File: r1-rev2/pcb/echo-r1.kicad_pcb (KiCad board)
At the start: 6 copper layers, 90.8 x 100.6 mm, 146 parts, among them J1 TYPE-C-31-M-12, J2 TF-115, J3 HP_3.5mm, J4 LO_3.5mm, J5 GT-BTP30003-xxxA-16A, J6 AFC07-S30ECA-00, Q1 AO3401A, Q2 AO3401A, Q3 AO3401A, Q4 AO3401A, Q5 AO3401A, SW1 A, SW10 SELECT, SW11 VOL+, SW12 VOL-, SW13 POWER, SW14 HOLD, SW2 B, SW3 X, SW4 Y, SW5 DPAD↑, SW6 DPAD↓, SW7 DPAD←, SW8 DPAD→, SW9 START, U1 STM32H7R3Z8Jx, U10 USBLC6-2SC6, U11 TPAZ1143-04F, U12 TPAZ1143-04F, U15 TPAZ1143-04F, U16 TPAZ1143-04F, U2 W958D8NBYA5I, U3 TLV320AIC3104, U4 LM66100DCK, U5 TPS62A01DRLR, U6 TPS62A01DRLR, U7 AP2125K-3.0, U8 AP2125K-3.0, U9 TP4057, Y1 SC-32S32.768kHz20PPM12.5pF, Y2 XTM32024000JT00351001

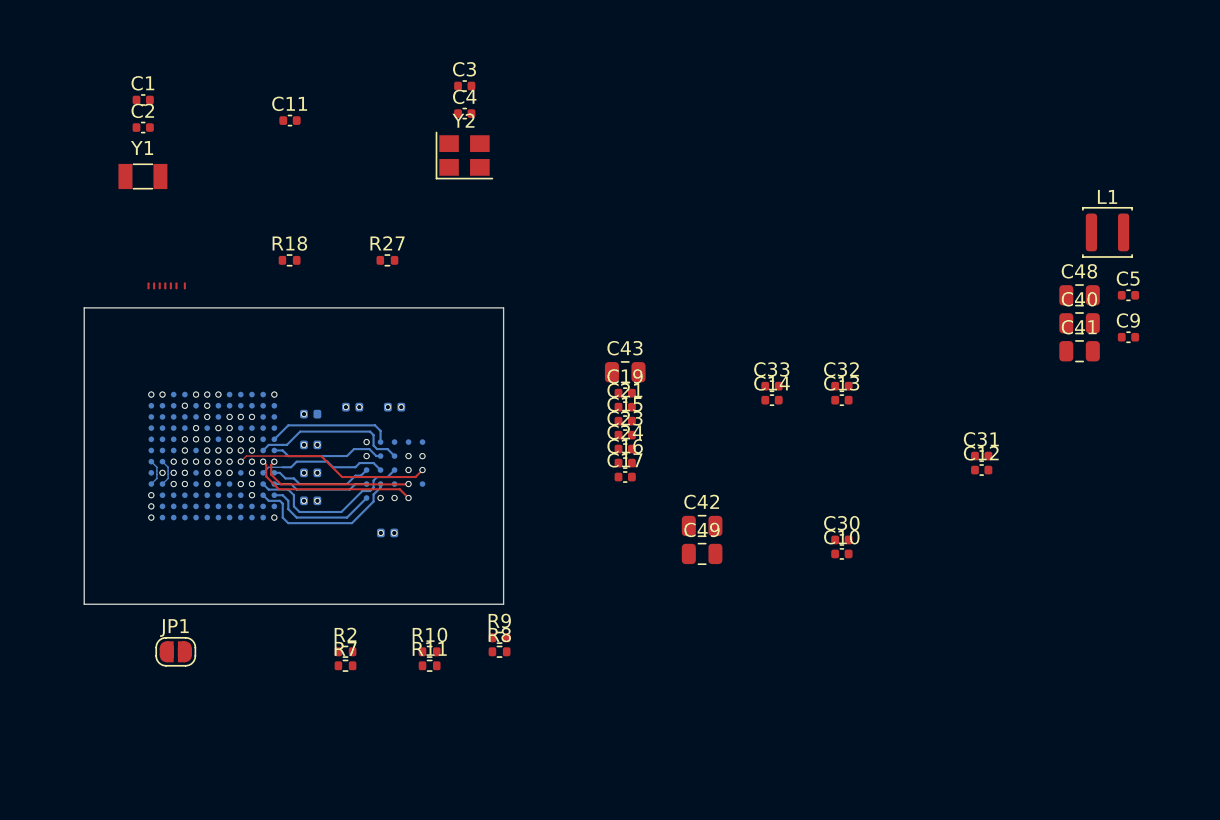
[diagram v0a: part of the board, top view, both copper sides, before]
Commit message: R1-Rev2: WIP STM32 crystal and SMPS layout
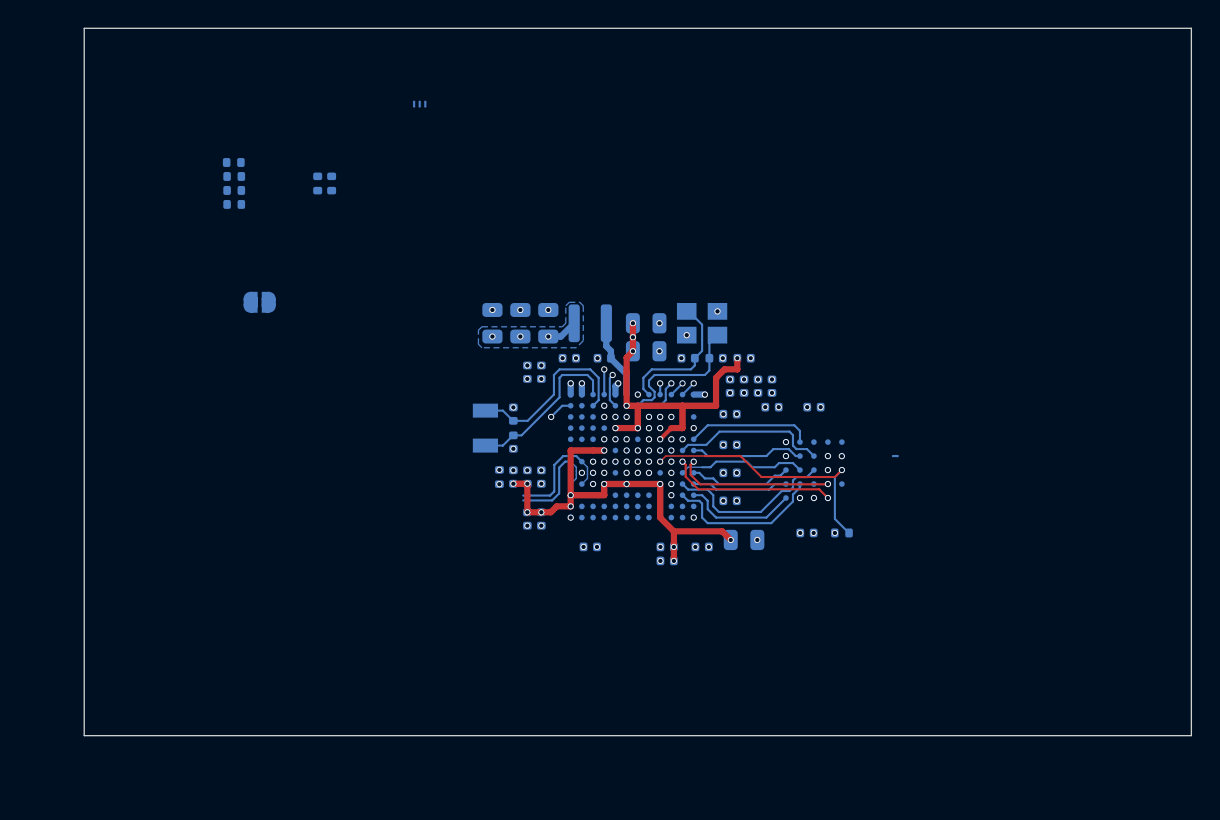
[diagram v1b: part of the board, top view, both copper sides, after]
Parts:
- removed NT10, NT4, NT5: NetTie_2, echoplayer:NetTie_0.15mm_SMD
- C1, C10, C11, C12, C13, C14, C15, C16, C17, C19, C2, C21, C23, C24, C3, C30, C31, C32, C33, C4, C40, C41, C42, C43, C48, C49, C5, C9, JP1, L1, NT1, NT11, NT6, NT7, R10, R11, R18, R2, R27, R7, R8, R9, Y1, Y2: moved to B.Cu
- moved NT11 52.3 mm to (240.3, 62.0), turned to 180 degrees
- moved C9 43.2 mm to (215.0, 63.5), turned to -90 degrees
- moved C11 42.4 mm to (226.5, 68.5)
- moved C41 42.0 mm to (211.5, 52.5), turned to 90 degrees
- moved C40 40.0 mm to (213.5, 52.5), turned to 90 degrees
- moved C48 38.1 mm to (215.5, 52.5), turned to 90 degrees
- moved R27 37.9 mm to (236.5, 67.5)
- moved C5 37.8 mm to (219.5, 55.0), turned to 180 degrees
- moved L1 37.6 mm to (218.5, 52.5)
- moved C1 36.1 mm to (213.0, 61.0), turned to -90 degrees
- moved R2 35.9 mm to (193.0, 41.0)
- moved R7 35.9 mm to (193.0, 42.0), turned to 180 degrees
- moved R10 35.8 mm to (193.0, 43.0), turned to 180 degrees
- moved R11 35.8 mm to (193.0, 44.0), turned to 180 degrees
- moved R8 35.6 mm to (200.0, 42.5), turned to -90 degrees
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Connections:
- U1 pad C8: /dvdd -> /vfbsmps
- U1 pad E5: /vcap -> /vfbsmps
- U1 pad F6: /vddldo -> /vfbsmps
- U1 pad F7: /vddldo -> /vfbsmps
- U1 pad F8: /vcap -> /vfbsmps
- U1 pad G6: /vddldo -> /vfbsmps
- U1 pad G7: /vddldo -> /vfbsmps
- U1 pad H6: /vcap -> /vfbsmps
- U1 pad H8: /vcap -> /vfbsmps
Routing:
- net +3V3: track 0.00 -> 53.9 mm, vias 10 -> 23
- net /vfbsmps: track 0.00 -> 32.9 mm, vias 1 -> 14
- net +1V8: track 26.2 -> 39.5 mm, vias 13 -> 14
- net /osc32k_out: track 0.00 -> 13.2 mm
- net +3V0_VBAT: track 0.00 -> 11.8 mm, vias 3 -> 9
- net /osc32k_in: track 0.00 -> 11.8 mm
- net /osc24m_in: track 0.00 -> 10.2 mm
- net /osc24m_out: track 0.00 -> 10.0 mm
- net /usb_d-: track 0.84 -> 7.48 mm
- net /vlxsmps: track 0.00 -> 5.70 mm, vias 1 -> 0
- net /usb_d+: track 0.84 -> 6.47 mm
- net /xspi.cs: track 14.0 -> 19.1 mm
- net GND: track 0.00 -> 2.48 mm, vias 30 -> 62
- net /codec.dplay: track 0.00 -> 2.45 mm, vias 0 -> 1
- net /lcd.d6: track 0.00 -> 1.93 mm, vias 0 -> 1
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- added copper zone on B.Cu, net /vfbsmps
- added copper zone on In3.Cu, net /vfbsmps
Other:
- board size 90.8 x 100.6 mm -> 140 x 120.6 mm

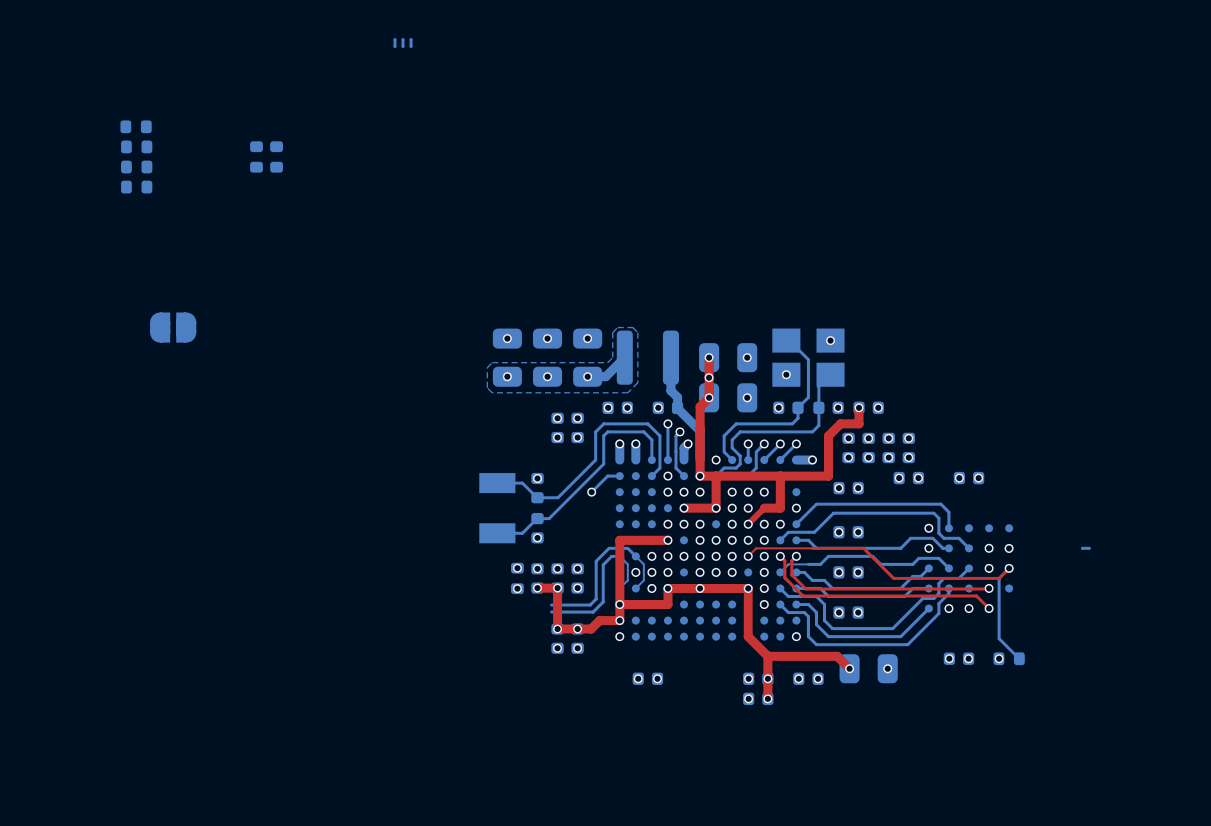
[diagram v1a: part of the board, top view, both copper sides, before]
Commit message: R1-Rev2: WIP STM32 signal and power routing
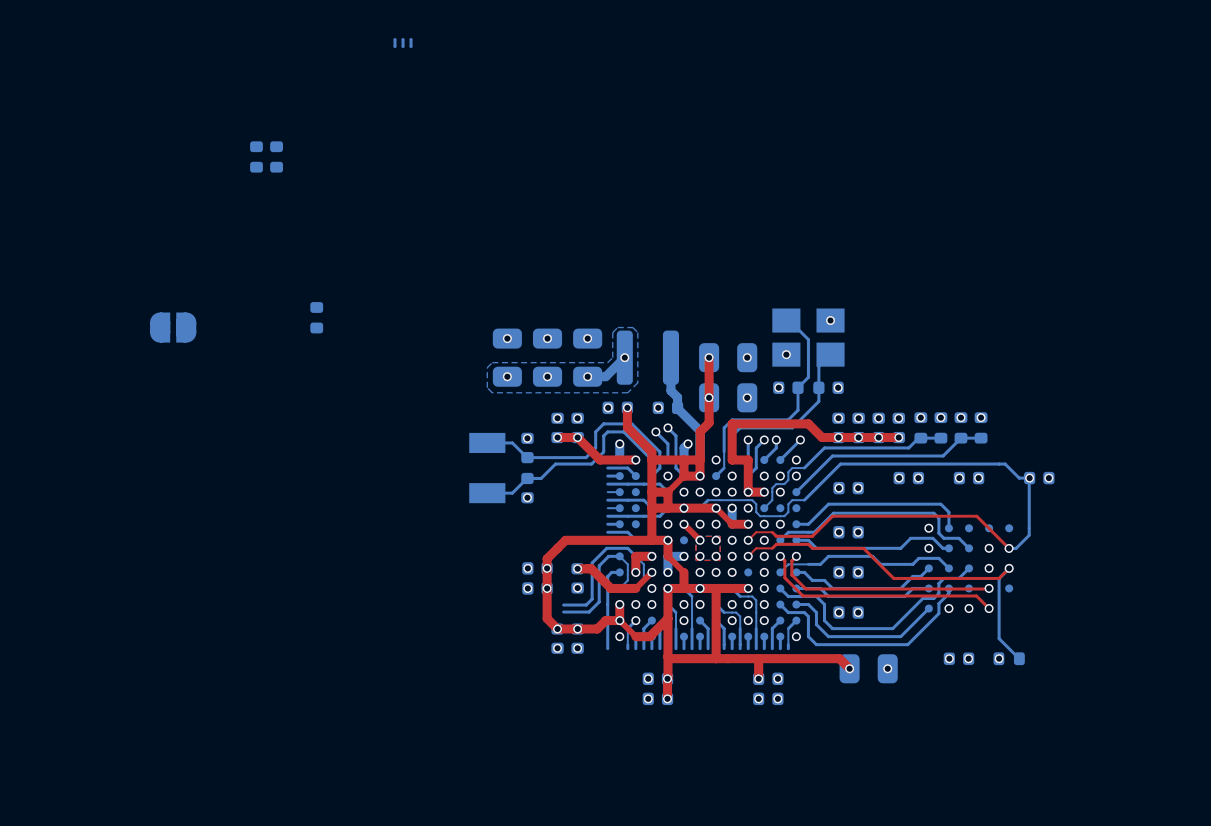
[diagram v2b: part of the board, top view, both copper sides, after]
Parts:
- moved R10 44.0 mm to (235.1, 56.0), turned to 90 degrees
- moved R2 42.8 mm to (233.1, 56.0), turned to -90 degrees
- moved R11 42.8 mm to (234.1, 56.0), turned to 90 degrees
- moved R7 41.5 mm to (232.1, 56.0), turned to 90 degrees
- moved R18 16.4 mm to (202.0, 50.5)
- moved C11 15.2 mm to (238.0, 58.5)
- moved C15 14.4 mm to (224.5, 68.5)
- moved C19 6.08 mm to (224.5, 69.5), turned to 0 degrees
- moved C17 5.00 mm to (219.0, 69.5)
- moved C21 5.00 mm to (219.0, 68.5)
- moved NT11 2.94 mm to (237.5, 61.2), turned to -90 degrees
- moved C3 2.24 mm to (225.5, 54.0), turned to 180 degrees
- moved C4 2.24 mm to (227.5, 54.0), turned to 0 degrees
- moved C1 2.06 mm to (212.5, 59.0)
- moved C2 2.06 mm to (212.5, 57.0)
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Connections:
- U1 pad A3: unconnected-(U1-PB6-PadA3) -> /sdmmc_pwr_en
- U1 pad A4: unconnected-(U1-PB5-PadA4) -> /sdmmc_detect
- U1 pad A8: unconnected-(U1-PM9-PadA8) -> /button_vol-
- U1 pad B12: unconnected-(U1-PD4-PadB12) -> /lcd_reset
- U1 pad B3: /sdmmc_pwr_en -> unconnected-(U1-PE1-PadB3)
- U1 pad B4: /sdmmc_detect -> unconnected-(U1-PE0-PadB4)
- U1 pad C3: /lcd_reset -> unconnected-(U1-PB9-PadC3)
- U1 pad D12: unconnected-(U1-PA15(JTDI)-PadD12) -> /chg_enable
- U1 pad E8: /button_power -> unconnected-(U1-PM0-PadE8)
- U1 pad G9: /chg_enable -> unconnected-(U1-PC7-PadG9)
- U1 pad J8: /button_vol- -> unconnected-(U1-PD8-PadJ8)
- U1 pad K11: unconnected-(U1-PD12-PadK11) -> /button_power
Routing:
- net /swd.nrst: track 0.00 -> 21.3 mm
- net /xspi_reset: track 0.00 -> 15.6 mm
- net +3V3: track 53.9 -> 68.4 mm, vias 23 -> 22
- net /adc_vbat: track 0.00 -> 10.8 mm
- net /adc_vbus: track 0.00 -> 10.3 mm
- net /lcd.dcx: track 0.00 -> 8.18 mm, vias 0 -> 1
- net /vfbsmps: track 32.9 -> 41.1 mm, vias 14 -> 15
- net +3V0_VBAT: track 11.8 -> 17.9 mm
- net /button_x: track 0.00 -> 5.91 mm
- net /button_up: track 0.00 -> 4.53 mm, vias 0 -> 1
- net /button_vol-: track 0.00 -> 4.28 mm
- net /uart_tx: track 0.00 -> 3.85 mm
- net /button_hold: track 0.00 -> 3.33 mm, vias 0 -> 1
- net /codec.wclk: track 0.00 -> 3.25 mm
- net /codec.drec: track 0.00 -> 3.17 mm, vias 1 -> 0
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- added copper zone on F.Cu, net /vfbsmps

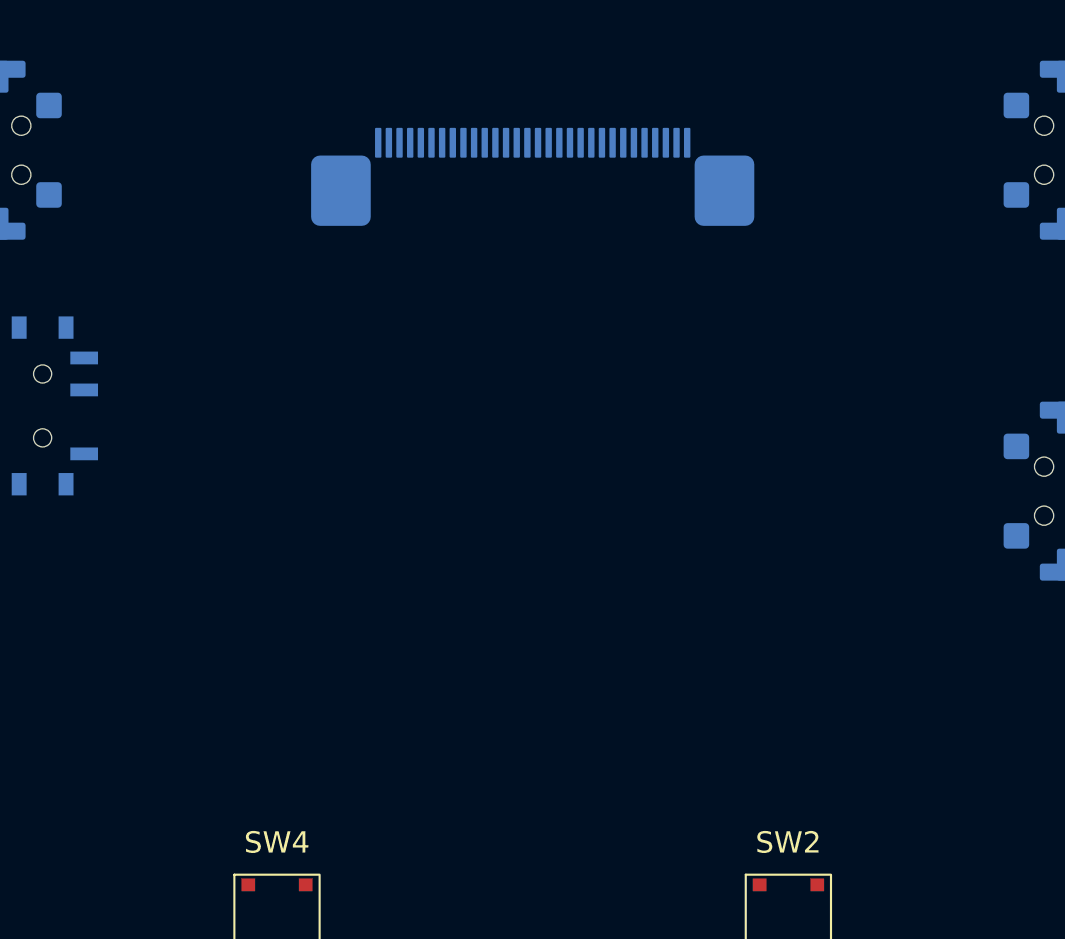
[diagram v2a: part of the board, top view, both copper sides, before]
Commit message: R1-Rev2: move LCD in Z-axis to free up board space
Mounting the LCD directly to the PCB just proved to be too
awkward; mainly because the connector position made it hard
to fit components on the upper half of the PCB. Mounting it
on top of a 1.2mm support which directly contacts the PCB
alleviates this, and the cable slot can now be smaller and
moved up closer to the connector. This provides a bit more
room everywhere and will make placement & routing simpler.

There is a slight impact on thickness, but the acrylic LCD
cover can be reduced in thickness to compensate.
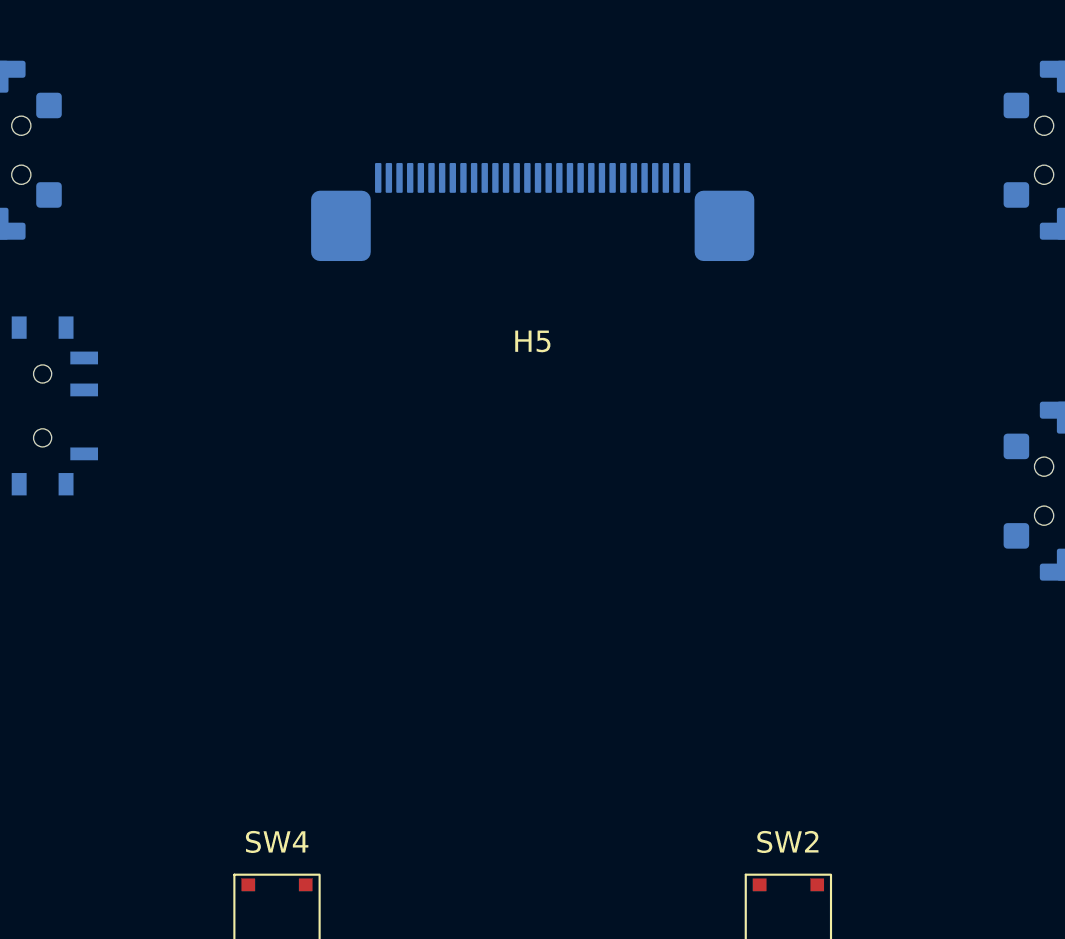
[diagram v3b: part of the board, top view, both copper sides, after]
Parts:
- H5: value 38x2mm -> 17x2mm; footprint echoplayer:Slot_38x2mm -> echoplayer:Slot_17x2mm; moved to F.Cu
- moved H5 19.0 mm to (147.5, 85.0), turned to 0 degrees
- moved J6 1.65 mm to (147.5, 76.0)
